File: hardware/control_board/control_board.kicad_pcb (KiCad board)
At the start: 2 copper layers, 80 x 80 mm, 126 parts, among them J1 SWD, J2 Aux, J3 Panel, J4 6.5/2mm, J5 USB_C, J6 RTD, J7 TC, J8 Conn_01x01, J9 Conn_01x01, Q1 2N7002A, Q2 IRF1018ESTRLPBF, SW1 Reset, SW2 Power, U1 STM32F103C8T6, U2 LMR38010SDDAR, U3 TLV76133DCYR, U4 USBLC6-2SC6, U5 MAX6675, U6 MCP6N11T-005E, U7 MCP6001T, U8 TLP183, Y1 8MHz

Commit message: Cleanup the project
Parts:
- C10: value 100n/35V -> 100n
- C9: value 4u7/35V -> 4u7
- D9: value SK36A -> SK310A
- FB1, FB2: value 470R@100MHz -> 470R
- R29: value 5k -> 4k99
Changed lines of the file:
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@@
         (effects (font (size 1 1) (thickness 0.15)))
     )
-    (fp_text value "5k" (at 0 1.43) (layer "F.Fab")
+    (fp_text value "4k99" (at 0 1.43) (layer "F.Fab")
         (effects (font (size 1 1) (thickness 0.15)))
     )
@@
       (stroke (width 0.1) (type solid)) (layer "F.Fab"))
     (pad "1" smd rect (at -3.15 -2.3 270) (size 2 1.5) (layers "F.Cu" "F.Paste" "F.Mask")
-      (net 2 "GND") (pinfunction "GND") (pintype "power_in"))
+      (net 2 "GND") (pinfunction "GND") (pintype "power_in") (thermal_bridge_width 2))
     (pad "2" smd rect (at -3.15 0 270) (size 2 1.5) (layers "F.Cu" "F.Paste" "F.Mask")
       (net 12 "+3.3V") (pinfunction "VO") (pintype "power_out"))
@@
     (descr "Capacitor SMD 0603 (1608 Metric), square (rectangular) end terminal, IPC_7351 nominal, (Body size source: IPC-SM-782 page 76, https://www.pcb-3d.com/wordpress/wp-content/uploads/ipc-sm-782a_amendment_1_and_2.pdf), generated with kicad-footprint-generator")
     (tags "capacitor")
+    (property "Rated Voltage" "35V")
     (property "Sheetfile" "power_supply.kicad_sch")
     (property "Sheetname" "Power Supply")
@@
         (effects (font (size 1 1) (thickness 0.15)) (justify left))
     )
-    (fp_text value "4u7/35V" (at 0 1.43 90) (layer "F.Fab")
+    (fp_text value "4u7" (at 0 1.43 90) (layer "F.Fab")
         (effects (font (size 1 1) (thickness 0.15)))
     )
@@
     (descr "Capacitor SMD 0603 (1608 Metric), square (rectangular) end terminal, IPC_7351 nominal, (Body size source: IPC-SM-782 page 76, https://www.pcb-3d.com/wordpress/wp-content/uploads/ipc-sm-782a_amendment_1_and_2.pdf), generated with kicad-footprint-generator")
     (tags "capacitor")
+    (property "Rated Voltage" "35V")
     (property "Sheetfile" "power_supply.kicad_sch")
     (property "Sheetname" "Power Supply")
@@
         (effects (font (size 1 1) (thickness 0.15)) (justify left))
     )
-    (fp_text value "100n/35V" (at 0 1.43 90) (layer "F.Fab")
+    (fp_text value "100n" (at 0 1.43 90) (layer "F.Fab")
         (effects (font (size 1 1) (thickness 0.15)))
     )
@@
         (effects (font (size 1 1) (thickness 0.15)))
     )
-    (fp_text value "SK36A" (at 0 2.6) (layer "F.Fab")
+    (fp_text value "SK310A" (at 0 2.6) (layer "F.Fab")
         (effects (font (size 1 1) (thickness 0.15)))
     )
@@
         (effects (font (size 1 1) (thickness 0.15)))
     )
-    (fp_text value "470R@100MHz" (at 0 1.43 90) (layer "F.Fab")
+    (fp_text value "470R" (at 0 1.43 90) (layer "F.Fab")
         (effects (font (size 1 1) (thickness 0.15)))
     )
@@
         (effects (font (size 1 1) (thickness 0.15)))
     )
-    (fp_text value "470R@100MHz" (at 0 1.43 90) (layer "F.Fab")
+    (fp_text value "470R" (at 0 1.43 90) (layer "F.Fab")
         (effects (font (size 1 1) (thickness 0.15)))
     )

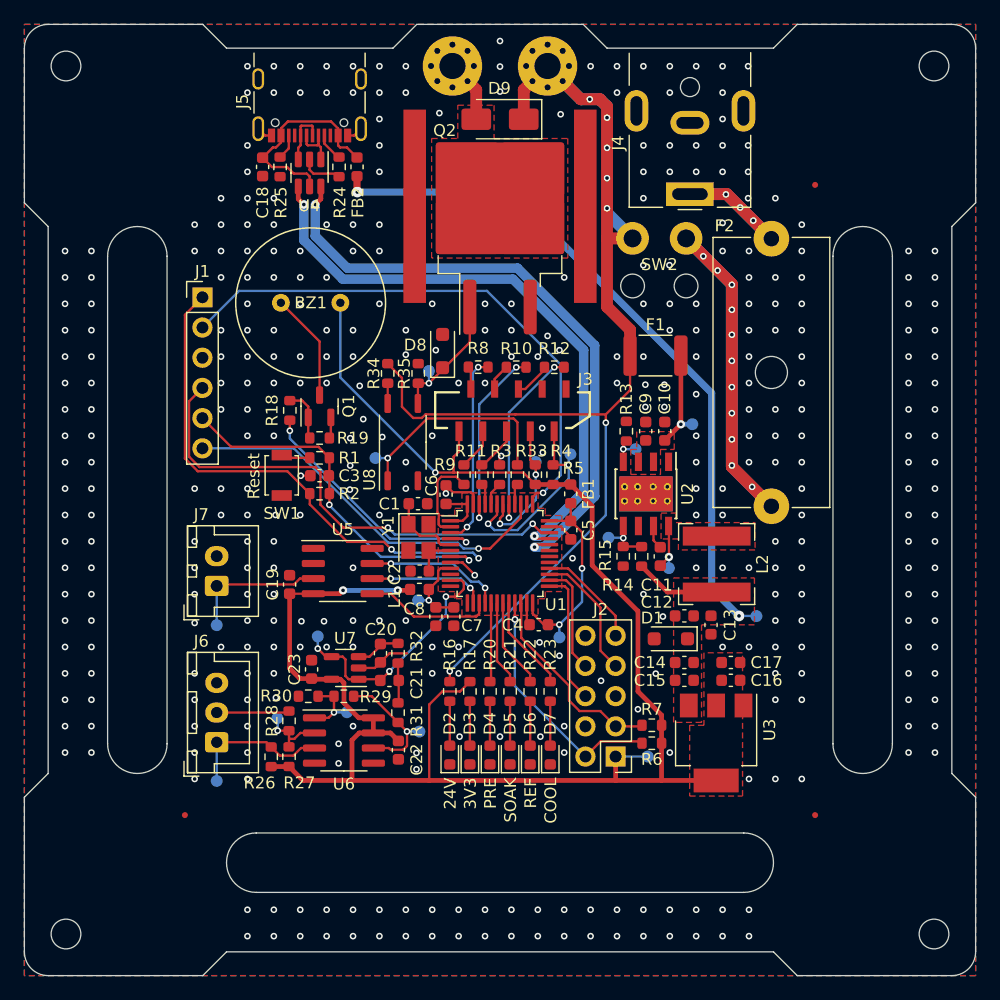
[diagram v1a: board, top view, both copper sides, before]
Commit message: Adjust fiducials
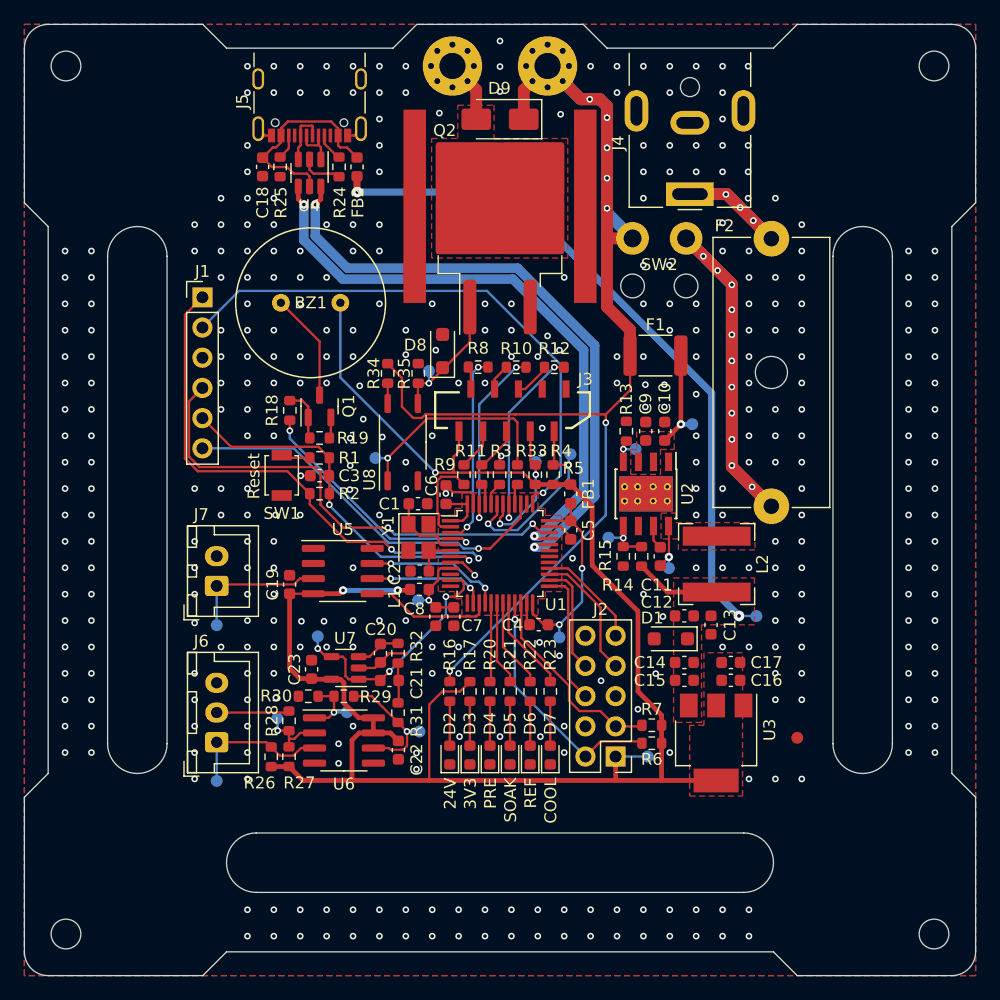
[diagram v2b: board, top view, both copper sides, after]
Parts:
- removed FID2, FID3: Fiducial, Fiducial:Fiducial_0.5mm_Mask1mm
- FID1: footprint Fiducial:Fiducial_0.5mm_Mask1mm -> Fiducial:Fiducial_1mm_Mask2mm
- moved FID1 51.9 mm to (173.0, 120.0)
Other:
- board text added: "20231113"
- board text removed: "20230914"
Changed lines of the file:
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@@
   (title_block
     (title "Reflow Hot Plate Control Board")
-    (date "2023-09-14")
+    (date "2023-11-13")
     (rev "${REVISION}")
     (company "Author: I. Kajdan")
@@
     )
   )
-  (property "REVISION" "1.0")
+  (property "REVISION" "1.1")
   (net 0 "")
   (net 1 "/HSE_IN")
@@
     )
   )
-  (footprint "Fiducial:Fiducial_0.5mm_Mask1mm" (layer "F.Cu")
-    (at 174.5 126.5)
-    (descr "Circular Fiducial, 0.5mm bare copper, 1mm soldermask opening (Level C)")
-    (tags "fiducial")
-    (property "Sheetfile" "mechanical.kicad_sch")
-    (property "Sheetname" "Mechanical Components")
-    (property "exclude_from_bom" "")
-    (property "ki_description" "Fiducial Marker")
-    (property "ki_keywords" "fiducial marker")
-    (attr smd exclude_from_bom)
-    (fp_text reference "FID2" (at 0 -1.5) (layer "F.SilkS") hide
-        (effects (font (size 1 1) (thickness 0.15)))
-    )
-    (fp_text value "Fiducial" (at 0 1.5) (layer "F.Fab")
-        (effects (font (size 1 1) (thickness 0.15)))
-    )
-    (fp_text user "${REFERENCE}" (at 0 0) (layer "F.Fab")
-        (effects (font (size 0.2 0.2) (thickness 0.04)))
-    )
-    (fp_circle (center 0 0) (end 0.75 0)
-      (stroke (width 0.05) (type solid)) (fill none) (layer "F.CrtYd"))
-    (fp_circle (center 0 0) (end 0.5 0)
-      (stroke (width 0.1) (type solid)) (fill none) (layer "F.Fab"))
-    (pad "" smd circle (at 0 0) (size 0.5 0.5) (layers "F.Cu" "F.Mask")
-      (solder_mask_margin 0.25) (clearance 0.25))
-  )
   (footprint "Local_Library:SwitchWireRelief" (layer "F.Cu")
     (at 159.15 78)
@@
     )
   )
-  (footprint "Fiducial:Fiducial_0.5mm_Mask1mm" (layer "F.Cu")
-    (at 174.5 73.5)
-    (descr "Circular Fiducial, 0.5mm bare copper, 1mm soldermask opening (Level C)")
-    (tags "fiducial")
-    (property "Sheetfile" "mechanical.kicad_sch")
-    (property "Sheetname" "Mechanical Components")
-    (property "exclude_from_bom" "")
-    (property "ki_description" "Fiducial Marker")
-    (property "ki_keywords" "fiducial marker")
-    (attr smd exclude_from_bom)
-    (fp_text reference "FID3" (at 0 -1.5) (layer "F.SilkS") hide
-        (effects (font (size 1 1) (thickness 0.15)))
-    )
-    (fp_text value "Fiducial" (at 0 1.5) (layer "F.Fab")
-        (effects (font (size 1 1) (thickness 0.15)))
-    )
-    (fp_text user "${REFERENCE}" (at 0 0) (layer "F.Fab")
-        (effects (font (size 0.2 0.2) (thickness 0.04)))
-    )
-    (fp_circle (center 0 0) (end 0.75 0)
-      (stroke (width 0.05) (type solid)) (fill none) (layer "F.CrtYd"))
-    (fp_circle (center 0 0) (end 0.5 0)
-      (stroke (width 0.1) (type solid)) (fill none) (layer "F.Fab"))
-    (pad "" smd circle (at 0 0) (size 0.5 0.5) (layers "F.Cu" "F.Mask")
-      (solder_mask_margin 0.25) (clearance 0.25))
-  )
   (footprint "Resistor_SMD:R_0603_1608Metric" (layer "F.Cu")
     (at 139.425 117.885 90)
@@
     )
   )
-  (footprint "Fiducial:Fiducial_0.5mm_Mask1mm" (layer "F.Cu")
-    (at 121.5 126.5)
-    (descr "Circular Fiducial, 0.5mm bare copper, 1mm soldermask opening (Level C)")
+  (footprint "Fiducial:Fiducial_1mm_Mask2mm" (layer "F.Cu")
+    (at 173 120)
+    (descr "Circular Fiducial, 1mm bare copper, 2mm soldermask opening (Level A)")
     (tags "fiducial")
     (property "Sheetfile" "mechanical.kicad_sch")
@@
     (property "ki_keywords" "fiducial marker")
     (attr smd exclude_from_bom)
-    (fp_text reference "FID1" (at 0 -1.5) (layer "F.SilkS") hide
+    (fp_text reference "FID1" (at 0 -2) (layer "F.SilkS") hide
         (effects (font (size 1 1) (thickness 0.15)))
     )
-    (fp_text value "Fiducial" (at 0 1.5) (layer "F.Fab")
+    (fp_text value "Fiducial" (at 0 2) (layer "F.Fab")
         (effects (font (size 1 1) (thickness 0.15)))
     )
     (fp_text user "${REFERENCE}" (at 0 0) (layer "F.Fab")
-        (effects (font (size 0.2 0.2) (thickness 0.04)))
+        (effects (font (size 0.4 0.4) (thickness 0.06)))
     )
-    (fp_circle (center 0 0) (end 0.75 0)
+    (fp_circle (center 0 0) (end 1.25 0)
       (stroke (width 0.05) (type solid)) (fill none) (layer "F.CrtYd"))
-    (fp_circle (center 0 0) (end 0.5 0)
+    (fp_circle (center 0 0) (end 1 0)
       (stroke (width 0.1) (type solid)) (fill none) (layer "F.Fab"))
-    (pad "" smd circle (at 0 0) (size 0.5 0.5) (layers "F.Cu" "F.Mask")
-      (solder_mask_margin 0.25) (clearance 0.25))
+    (pad "" smd circle (at 0 0) (size 1 1) (layers "F.Cu" "F.Mask")
+      (solder_mask_margin 0.5) (clearance 0.5))
   )
   (footprint "Resistor_SMD:R_0603_1608Metric" (layer "F.Cu")
@@
   (gr_line locked (start 176 120.5) (end 176 79.5)
     (stroke (width 0.1) (type default)) (layer "Edge.Cuts"))
-  (gr_text "20230914" (at 164 71.35) (layer "B.SilkS")
+  (gr_text "20231113" (at 164 71.35) (layer "B.SilkS")
     (effects (font (size 1 1) (thickness 0.15)) (justify mirror))
   )

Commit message: Change the buzzer
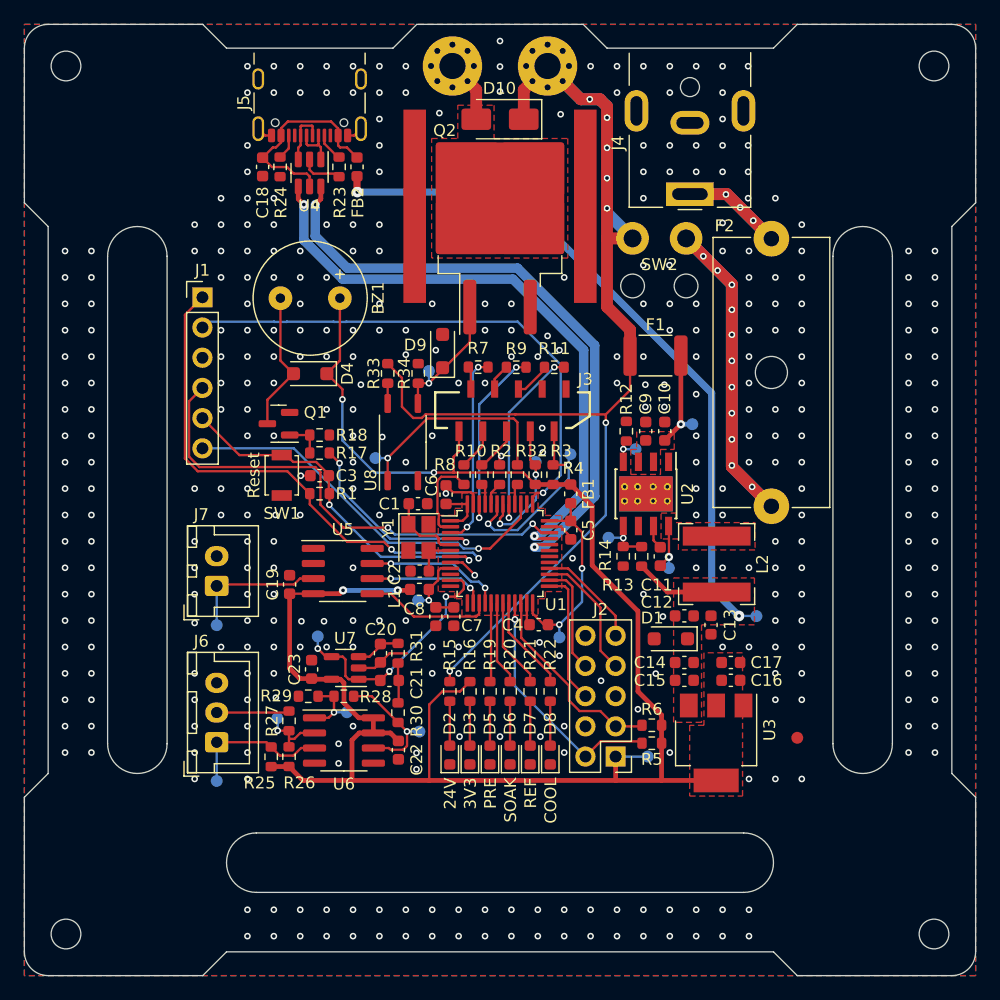
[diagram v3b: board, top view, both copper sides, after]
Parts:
- removed the R1 at (132.8, 96.5)
- added D4: MBR1020VL, Diode_SMD:D_SOD-123F, F.Cu at (132.0, 89.4)
- BZ1: footprint Local_Library:PKM13EPYH4000-A0 -> Local_Library:CMI-9605IC-0380T
- J5: footprint Connector_USB:USB_C_Receptacle_GCT_USB4105-xx-A_16P_TopMnt_Horizontal -> Local_Library:USB4105-GF-A
- moved R17 4.37 mm to (132.8, 96.0), turned to 0 degrees
- moved Q1 3.75 mm to (129.4, 93.6), turned to 180 degrees
- moved BZ1 0.39 mm to (132.0, 83.0), turned to -90 degrees
- moved R18 0.25 mm to (132.8, 94.5)
- renumbered D9 to D10, D4 to D5, D5 to D6, D6 to D7, D7 to D8, D8 to D9, R2 to R1, R11 to R10, R12 to R11, R13 to R12, R14 to R13, R15 to R14, R16 to R15, R17 to R16, R18 to R17, R19 to R18, R20 to R19, R3 to R2, R21 to R20, R22 to R21, R23 to R22, R24 to R23, R25 to R24, R26 to R25, R27 to R26, R28 to R27, R29 to R28, R30 to R29, R4 to R3, R31 to R30, R32 to R31, R33 to R32, R34 to R33, R35 to R34, R5 to R4, R6 to R5, R7 to R6, R8 to R7, R9 to R8, R10 to R9
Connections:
- SW1 pad 2: Net-(R1-Pad2) -> /NRST
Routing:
- net +3.3V: track 149.7 -> 154.1 mm, vias 3 -> 4
- net /BUZZER: track 21.4 -> 17.3 mm
- net Net-(D4-A): track 9.11 -> 12.7 mm
- net Net-(R1-Pad2): track 2.45 -> 0.00 mm
- net /SWCLK: track 47.0 -> 44.9 mm
- net GND: track 25.2 -> 23.4 mm, vias 383 -> 384
- net Net-(Q1-G): track 4.45 -> 3.20 mm
- net /NRST: track 31.5 -> 30.6 mm

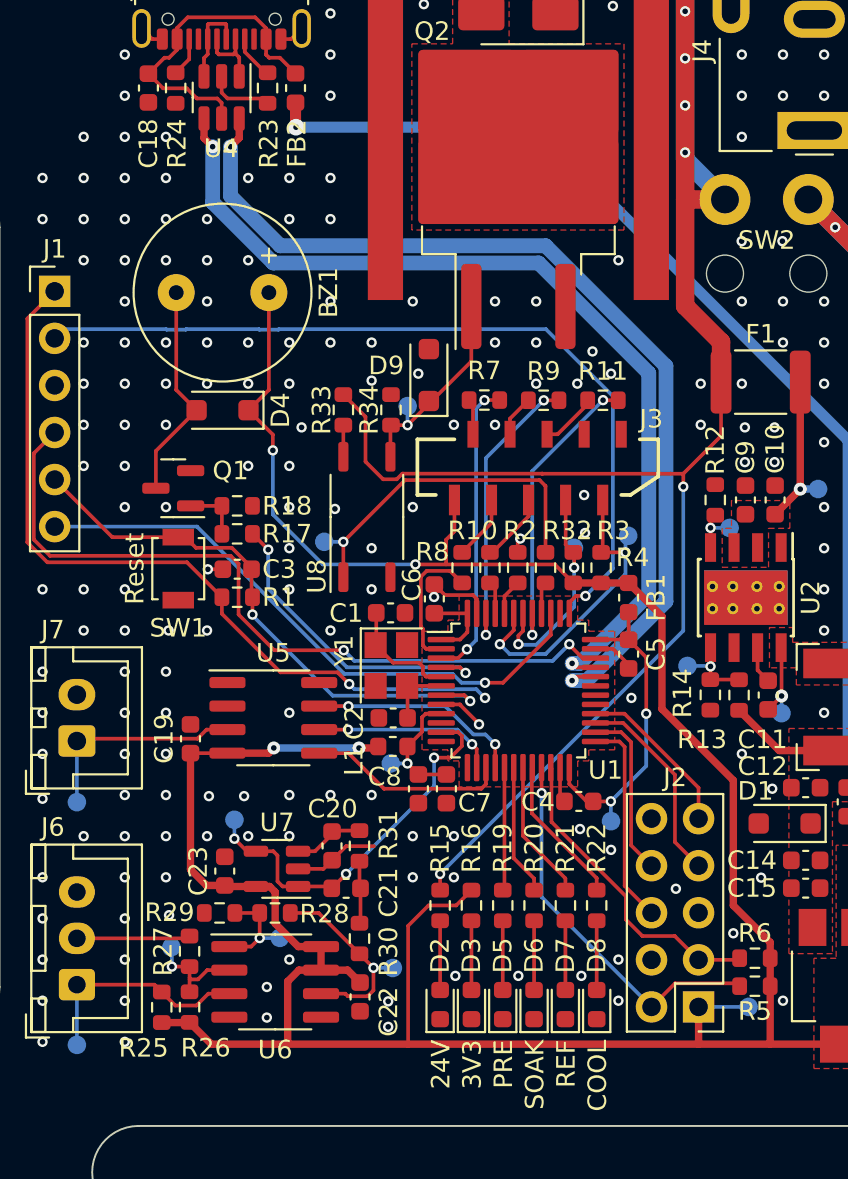
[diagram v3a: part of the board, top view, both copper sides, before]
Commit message: Add USB D+ pull-up resistor
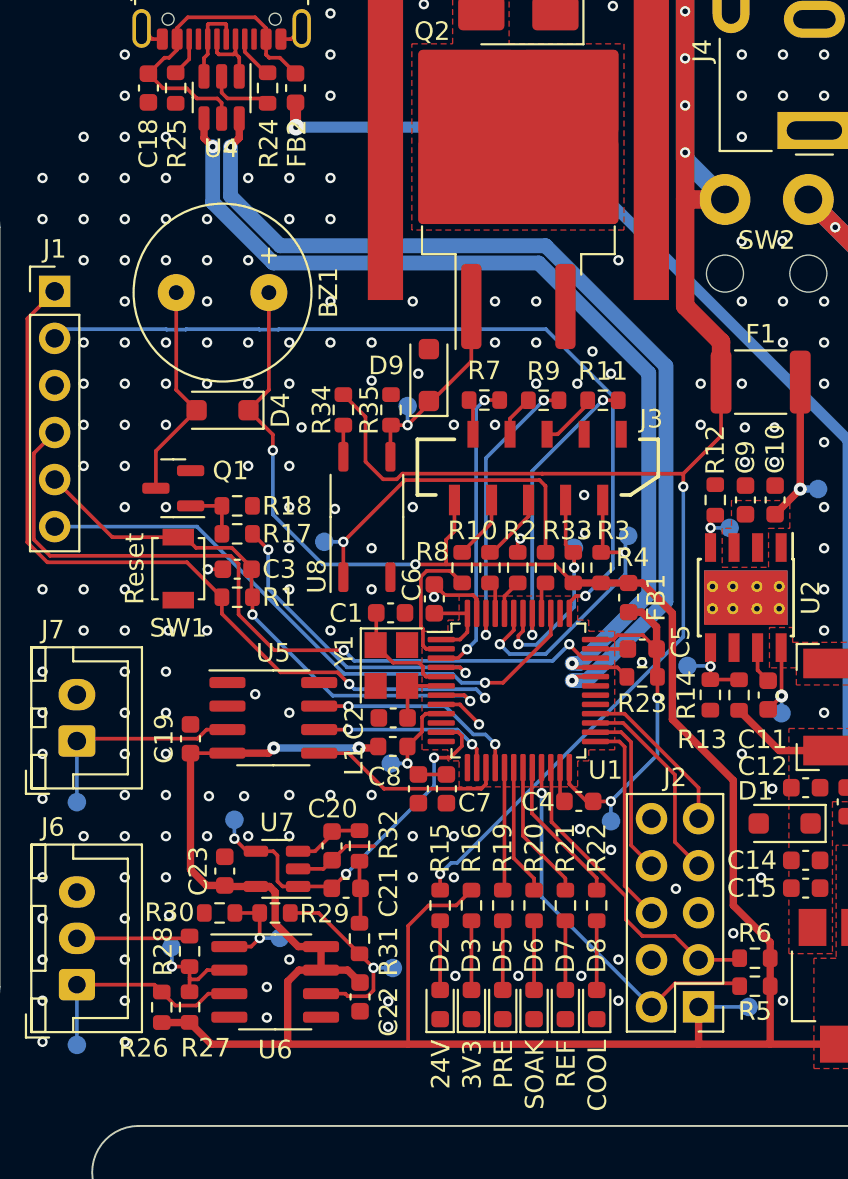
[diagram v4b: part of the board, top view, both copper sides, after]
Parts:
- removed the REF** at (131.2, 123.6)
- added R23: 1k5, Resistor_SMD:R_0603_1608Metric, F.Cu at (154.7, 103.8)
- added REF**: OSHW-Symbol_6.7x6mm_SilkScreen, Local_Library:OSHW-Symbol_6.7x6mm_SilkScreen, B.Cu at (131.6, 123.2)
- moved C5 0.78 mm to (154.7, 102.3), turned to 180 degrees
- renumbered R23 to R24, R24 to R25, R25 to R26, R26 to R27, R27 to R28, R28 to R29, R29 to R30, R30 to R31, R31 to R32, R32 to R33, R33 to R34, R34 to R35
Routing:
- net VDD: track 65.0 -> 67.8 mm
- net /USB_D+: track 51.0 -> 52.9 mm
- net GND: track 23.4 -> 22.8 mm, vias 384 -> 385

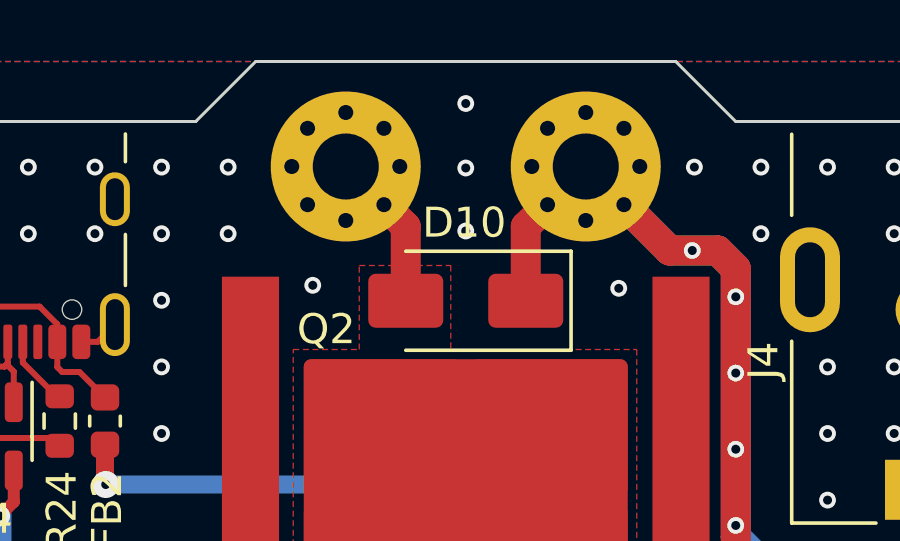
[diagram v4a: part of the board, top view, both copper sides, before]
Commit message: Use Schottky flyback diode for heatbed
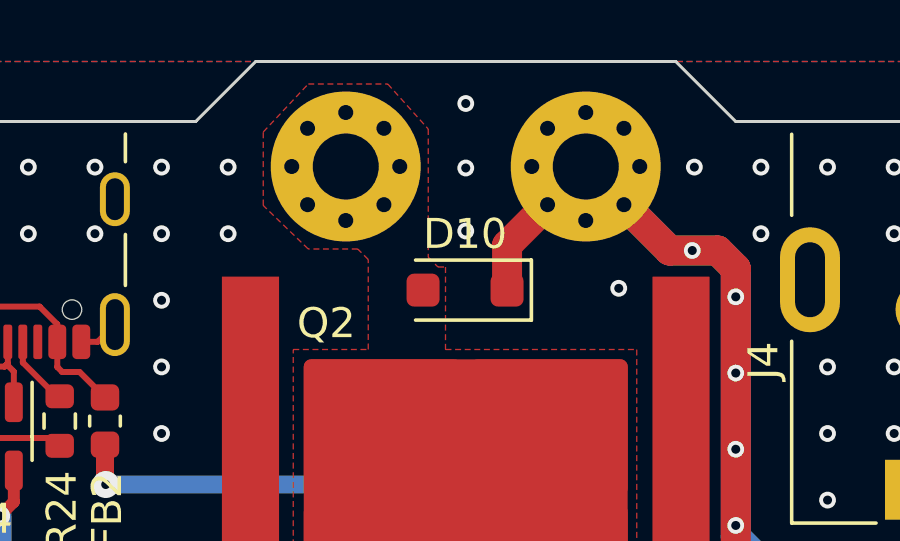
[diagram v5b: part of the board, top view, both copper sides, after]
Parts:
- D10: value SK310A -> SKL310; footprint Diode_SMD:D_SMA -> Diode_SMD:D_SOD-123F
- R23: value 1k5 -> 1k47
- moved D10 0.36 mm to (148.0, 67.6)
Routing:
- net Net-(D10-A): track 5.30 -> 0.00 mm
- net GND: vias 385 -> 384
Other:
- board text added: "20231114"
- board text removed: "20231113"
